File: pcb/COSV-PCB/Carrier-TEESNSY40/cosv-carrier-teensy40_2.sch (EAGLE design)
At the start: 21 parts, among them K1 61200821621, K2 61200821621, K3 61200821621

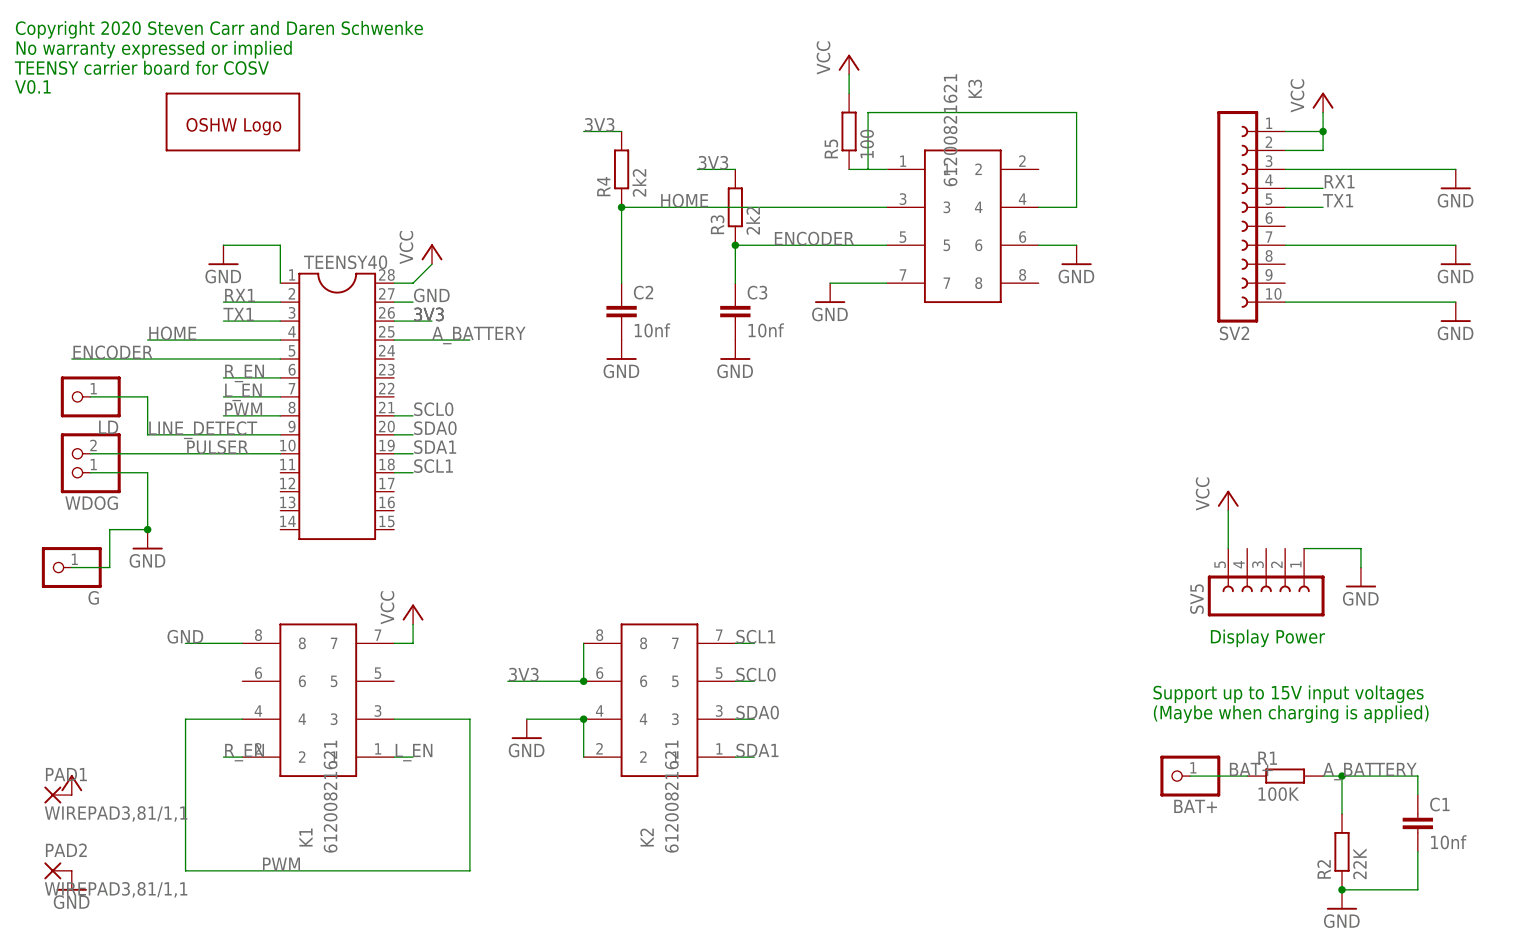
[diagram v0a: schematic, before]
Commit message: Routed for easier milling
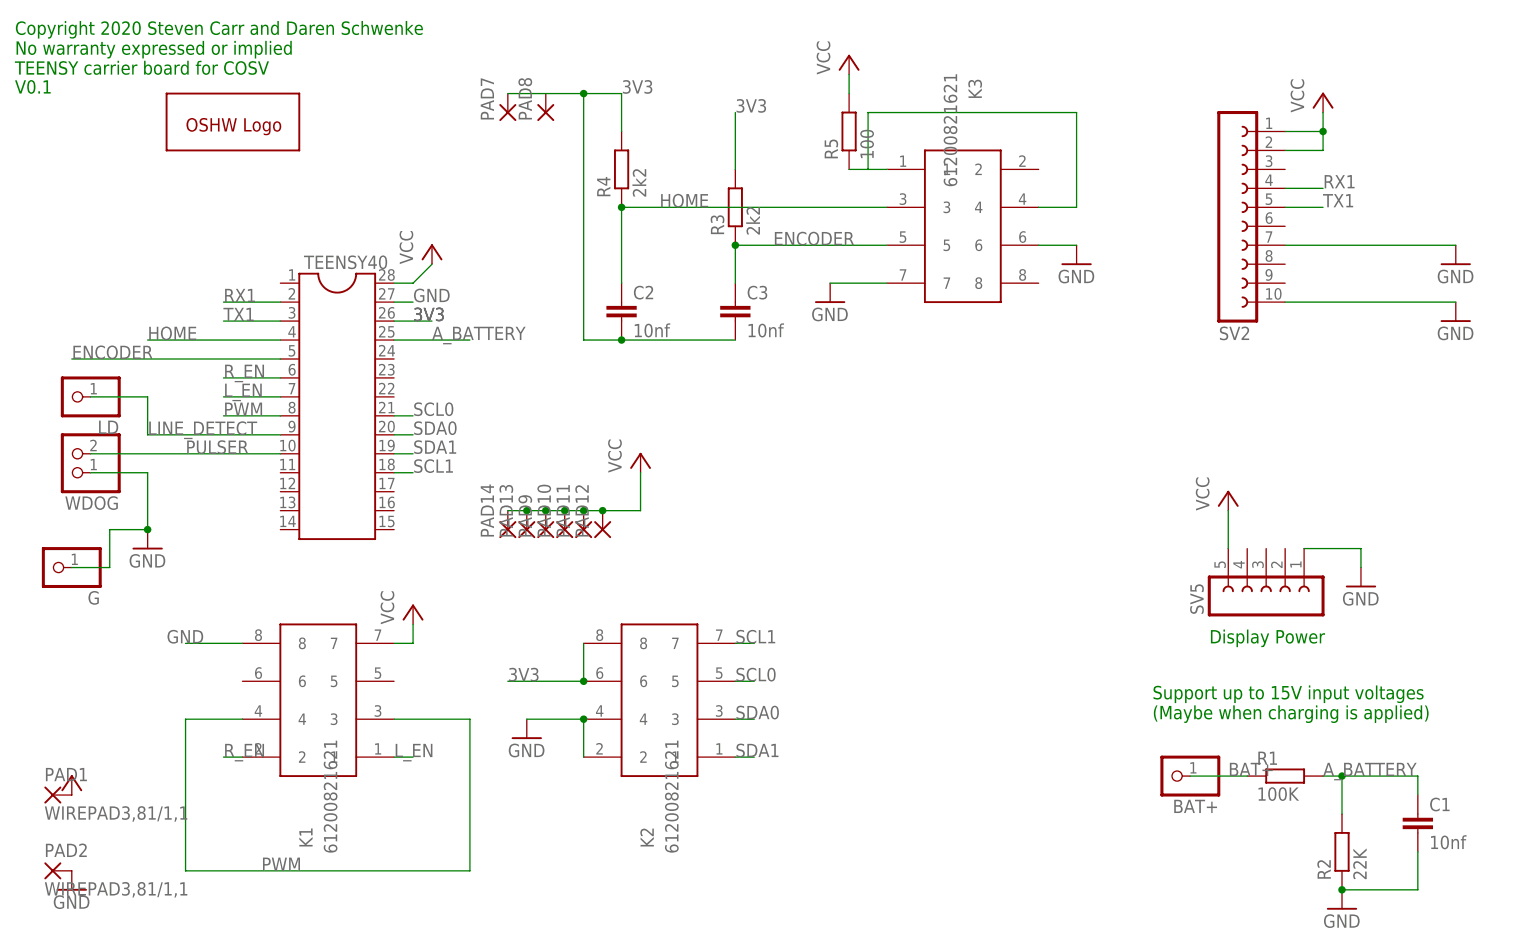
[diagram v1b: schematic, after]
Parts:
- added PAD10, PAD11, PAD12, PAD13, PAD14, PAD7, PAD8, PAD9: (no value), wirepad:1,6/0,9
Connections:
- net N$1 renamed LED
- net 3V3: now also C2.2, C3.2, PAD7.P, PAD8.P
- net GND: no longer C2.2, C3.2, SV2.3, TEENSY40.1
- net VCC: now also PAD10.P, PAD11.P, PAD12.P, PAD13.P, PAD14.P, PAD9.P
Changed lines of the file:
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@@
 <part name="P+3" library="supply1" deviceset="VCC" device=""/>
 <part name="P+6" library="supply1" deviceset="VCC" device=""/>
-<part name="GND6" library="supply1" deviceset="GND" device=""/>
 <part name="GND7" library="supply1" deviceset="GND" device=""/>
 <part name="GND4" library="supply1" deviceset="GND" device=""/>
@@
 <part name="GND20" library="supply1" deviceset="GND" device=""/>
 <part name="G" library="pinhead-2" deviceset="PINHD-1X01" device="_2.54-S"/>
-<part name="GND21" library="supply1" deviceset="GND" device=""/>
-<part name="GND12" library="supply1" deviceset="GND" device=""/>
 <part name="LD" library="pinhead-2" deviceset="PINHD-1X01" device="_2.54-S"/>
 <part name="C2" library="rcl" deviceset="C-EU" device="C1206" value="10nf"/>
@@
 <part name="P+5" library="supply1" deviceset="VCC" device=""/>
 <part name="GND5" library="supply1" deviceset="GND" device=""/>
-<part name="GND8" library="supply1" library_urn="urn:adsk.eagle:library:371" deviceset="GND" device=""/>
+<part name="P+7" library="supply1" library_urn="urn:adsk.eagle:library:371" deviceset="VCC" device=""/>
+<part name="PAD7" library="wirepad" library_urn="urn:adsk.eagle:library:412" deviceset="1,6/0,9" device="" package3d_urn="urn:adsk.eagle:package:30840/1"/>
+<part name="PAD8" library="wirepad" library_urn="urn:adsk.eagle:library:412" deviceset="1,6/0,9" device="" package3d_urn="urn:adsk.eagle:package:30840/1"/>
+<part name="PAD9" library="wirepad" library_urn="urn:adsk.eagle:library:412" deviceset="1,6/0,9" device="" package3d_urn="urn:adsk.eagle:package:30840/1"/>
+<part name="PAD10" library="wirepad" library_urn="urn:adsk.eagle:library:412" deviceset="1,6/0,9" device="" package3d_urn="urn:adsk.eagle:package:30840/1"/>
+<part name="PAD11" library="wirepad" library_urn="urn:adsk.eagle:library:412" deviceset="1,6/0,9" device="" package3d_urn="urn:adsk.eagle:package:30840/1"/>
+<part name="PAD12" library="wirepad" library_urn="urn:adsk.eagle:library:412" deviceset="1,6/0,9" device="" package3d_urn="urn:adsk.eagle:package:30840/1"/>
+<part name="PAD13" library="wirepad" library_urn="urn:adsk.eagle:library:412" deviceset="1,6/0,9" device="" package3d_urn="urn:adsk.eagle:package:30840/1"/>
+<part name="PAD14" library="wirepad" library_urn="urn:adsk.eagle:library:412" deviceset="1,6/0,9" device="" package3d_urn="urn:adsk.eagle:package:30840/1"/>
 </parts>
 <sheets>
@@
 <attribute name="VALUE" x="175.26" y="109.22" size="1.778" layer="96" rot="R90"/>
 </instance>
-<instance part="GND6" gate="1" x="195.58" y="99.06" smashed="yes">
-<attribute name="VALUE" x="193.04" y="96.52" size="1.778" layer="96"/>
-</instance>
 <instance part="GND7" gate="1" x="195.58" y="88.9" smashed="yes">
 <attribute name="VALUE" x="193.04" y="86.36" size="1.778" layer="96"/>
@@
 <attribute name="VALUE" x="13.97" y="53.34" size="1.778" layer="96" rot="R180"/>
 </instance>
-<instance part="GND21" gate="1" x="99.06" y="76.2" smashed="yes">
-<attribute name="VALUE" x="96.52" y="73.66" size="1.778" layer="96"/>
-</instance>
-<instance part="GND12" gate="1" x="83.82" y="76.2" smashed="yes">
-<attribute name="VALUE" x="81.28" y="73.66" size="1.778" layer="96"/>
-</instance>
 <instance part="LD" gate="A" x="10.16" y="71.12" smashed="yes" rot="R180">
 <attribute name="NAME" x="16.51" y="67.945" size="1.778" layer="95" rot="R180"/>
@@
 <attribute name="VALUE" x="142.24" y="86.36" size="1.778" layer="96"/>
 </instance>
-<instance part="GND8" gate="1" x="30.48" y="88.9" smashed="yes">
-<attribute name="VALUE" x="27.94" y="86.36" size="1.778" layer="96"/>
+<instance part="P+7" gate="VCC" x="86.36" y="63.5" smashed="yes">
+<attribute name="VALUE" x="83.82" y="60.96" size="1.778" layer="96" rot="R90"/>
+</instance>
+<instance part="PAD7" gate="1" x="68.58" y="109.22" smashed="yes" rot="R90">
+<attribute name="NAME" x="66.7258" y="108.077" size="1.778" layer="95" rot="R90"/>
+<attribute name="VALUE" x="71.882" y="108.077" size="1.778" layer="96" rot="R90"/>
+</instance>
+<instance part="PAD8" gate="1" x="73.66" y="109.22" smashed="yes" rot="R90">
+<attribute name="NAME" x="71.8058" y="108.077" size="1.778" layer="95" rot="R90"/>
+<attribute name="VALUE" x="76.962" y="108.077" size="1.778" layer="96" rot="R90"/>
+</instance>
+<instance part="PAD9" gate="1" x="73.66" y="53.34" smashed="yes" rot="R90">
+<attribute name="NAME" x="71.8058" y="52.197" size="1.778" layer="95" rot="R90"/>
+<attribute name="VALUE" x="76.962" y="52.197" size="1.778" layer="96" rot="R90"/>
+</instance>
+<instance part="PAD10" gate="1" x="76.2" y="53.34" smashed="yes" rot="R90">
+<attribute name="NAME" x="74.3458" y="52.197" size="1.778" layer="95" rot="R90"/>
+<attribute name="VALUE" x="79.502" y="52.197" size="1.778" layer="96" rot="R90"/>
+</instance>
+<instance part="PAD11" gate="1" x="78.74" y="53.34" smashed="yes" rot="R90">
+<attribute name="NAME" x="76.8858" y="52.197" size="1.778" layer="95" rot="R90"/>
+<attribute name="VALUE" x="82.042" y="52.197" size="1.778" layer="96" rot="R90"/>
+</instance>
+<instance part="PAD12" gate="1" x="81.28" y="53.34" smashed="yes" rot="R90">
+<attribute name="NAME" x="79.4258" y="52.197" size="1.778" layer="95" rot="R90"/>
+<attribute name="VALUE" x="84.582" y="52.197" size="1.778" layer="96" rot="R90"/>
+</instance>
+<instance part="PAD13" gate="1" x="71.12" y="53.34" smashed="yes" rot="R90">
+<attribute name="NAME" x="69.2658" y="52.197" size="1.778" layer="95" rot="R90"/>
+<attribute name="VALUE" x="74.422" y="52.197" size="1.778" layer="96" rot="R90"/>
+</instance>
+<instance part="PAD14" gate="1" x="68.58" y="53.34" smashed="yes" rot="R90">
+<attribute name="NAME" x="66.7258" y="52.197" size="1.778" layer="95" rot="R90"/>
+<attribute name="VALUE" x="71.882" y="52.197" size="1.778" layer="96" rot="R90"/>
 </instance>
 </instances>
@@
 <wire x1="114.3" y1="114.3" x2="114.3" y2="111.76" width="0.1524" layer="91"/>
 </segment>
+<segment>
+<pinref part="PAD14" gate="1" pin="P"/>
+<pinref part="PAD13" gate="1" pin="P"/>
+<wire x1="68.58" y1="55.88" x2="71.12" y2="55.88" width="0.1524" layer="91"/>
+<pinref part="PAD9" gate="1" pin="P"/>
+<wire x1="73.66" y1="55.88" x2="71.12" y2="55.88" width="0.1524" layer="91"/>
+<junction x="71.12" y="55.88"/>
+<pinref part="PAD10" gate="1" pin="P"/>
+<wire x1="73.66" y1="55.88" x2="76.2" y2="55.88" width="0.1524" layer="91"/>
+<junction x="73.66" y="55.88"/>
+<pinref part="PAD11" gate="1" pin="P"/>
+<wire x1="76.2" y1="55.88" x2="78.74" y2="55.88" width="0.1524" layer="91"/>
+<junction x="76.2" y="55.88"/>
+<pinref part="PAD12" gate="1" pin="P"/>
+<wire x1="78.74" y1="55.88" x2="81.28" y2="55.88" width="0.1524" layer="91"/>
+<junction x="78.74" y="55.88"/>
+<pinref part="P+7" gate="VCC" pin="VCC"/>
+<wire x1="81.28" y1="55.88" x2="86.36" y2="55.88" width="0.1524" layer="91"/>
+<wire x1="86.36" y1="55.88" x2="86.36" y2="60.96" width="0.1524" layer="91"/>
+<junction x="81.28" y="55.88"/>
+</segment>
 </net>
 <net name="GND" class="0">
@@
 <wire x1="175.26" y1="50.8" x2="182.88" y2="50.8" width="0.1524" layer="91"/>
 <wire x1="182.88" y1="50.8" x2="182.88" y2="48.26" width="0.1524" layer="91"/>
-</segment>
-<segment>
-<pinref part="GND6" gate="1" pin="GND"/>
-<wire x1="172.72" y1="101.6" x2="195.58" y2="101.6" width="0.1524" layer="91"/>
-<pinref part="SV2" gate="G$1" pin="3"/>
 </segment>
 <segment>
@@
 </segment>
 <segment>
-<pinref part="C2" gate="G$1" pin="2"/>
-<pinref part="GND12" gate="1" pin="GND"/>
-</segment>
-<segment>
-<pinref part="GND21" gate="1" pin="GND"/>
-<pinref part="C3" gate="G$1" pin="2"/>
-</segment>
-<segment>
 <pinref part="K3" gate="G$1" pin="6"/>
 <pinref part="GND5" gate="1" pin="GND"/>
 <wire x1="139.7" y1="91.44" x2="144.78" y2="91.44" width="0.1524" layer="91"/>
-</segment>
-<segment>
-<pinref part="TEENSY40" gate="G$1" pin="1"/>
-<pinref part="GND8" gate="1" pin="GND"/>
-<wire x1="38.1" y1="86.36" x2="38.1" y2="91.44" width="0.1524" layer="91"/>
-<wire x1="38.1" y1="91.44" x2="30.48" y2="91.44" width="0.1524" layer="91"/>
 </segment>
 </net>
@@
 </segment>
 <segment>
-<wire x1="78.74" y1="106.68" x2="83.82" y2="106.68" width="0.1524" layer="91"/>
-<label x="78.74" y="106.68" size="1.778" layer="95"/>
+<wire x1="83.82" y1="111.76" x2="83.82" y2="106.68" width="0.1524" layer="91"/>
+<label x="83.82" y="111.76" size="1.778" layer="95"/>
 <pinref part="R4" gate="G$1" pin="2"/>
-</segment>
-<segment>
-<wire x1="93.98" y1="101.6" x2="99.06" y2="101.6" width="0.1524" layer="91"/>
-<label x="93.98" y="101.6" size="1.778" layer="95"/>
+<wire x1="73.66" y1="111.76" x2="68.58" y2="111.76" width="0.1524" layer="91"/>
+<pinref part="PAD7" gate="1" pin="P"/>
+<wire x1="83.82" y1="111.76" x2="78.74" y2="111.76" width="0.1524" layer="91"/>
+<pinref part="PAD8" gate="1" pin="P"/>
+<pinref part="C2" gate="G$1" pin="2"/>
+<wire x1="78.74" y1="111.76" x2="73.66" y2="111.76" width="0.1524" layer="91"/>
+<wire x1="83.82" y1="78.74" x2="78.74" y2="78.74" width="0.1524" layer="91"/>
+<wire x1="78.74" y1="78.74" x2="78.74" y2="111.76" width="0.1524" layer="91"/>
+<junction x="78.74" y="111.76"/>
+<pinref part="C3" gate="G$1" pin="2"/>
+<wire x1="99.06" y1="78.74" x2="83.82" y2="78.74" width="0.1524" layer="91"/>
+<junction x="83.82" y="78.74"/>
+</segment>
+<segment>
+<wire x1="99.06" y1="109.22" x2="99.06" y2="101.6" width="0.1524" layer="91"/>
+<label x="99.06" y="109.22" size="1.778" layer="95"/>
 <pinref part="R3" gate="G$1" pin="2"/>
 </segment>
@@
 </segment>
 </net>
-<net name="N$1" class="0">
+<net name="LED" class="0">
 <segment>
 <pinref part="K3" gate="G$1" pin="1"/>
@@
 will not be understood (or retained) with this version.
 </note>
+<note version="8.3" severity="warning">
+Since Version 8.3, EAGLE supports the association of 3D packages
+with devices in libraries, schematics, and board files. Those 3D
+packages will not be understood (or retained) with this version.
+</note>
 </compatibility>
